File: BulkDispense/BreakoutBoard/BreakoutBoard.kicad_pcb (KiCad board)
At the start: 2 copper layers, 80 x 80 mm, 30 parts, among them J1 PS, J10 R0~R5, J11 WL1, J12 WL2, J13 DigitalOUT 0~3, J14 DigitalOUT 4~7, J15 WB1, J16 WB2, J17 AnalogIOs, J18 WB-MV1&2, J19 WB-MV3&4, J2 MV1&2, J20 FS1, J21 FS2~FS4, J22 WB-MV5&6, J24 LDS, J3 MV3&4, J4 RV1~4, J5 PCV, J6 FS1, J7 FS3, J8 FS2, J9 FS4

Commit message: Add updated layout
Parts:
- J11, J12, J15, J16, J22: footprint PartsLibrary:CONN_37203-62A3-003PL_3MM -> PartsLibrary:CONN_37204-62A3-004PL_3MM
- moved J22 2.27 mm to (142.6, 45.3)
- moved J16 2.05 mm to (152.5, 47.8)
- moved J15 2.00 mm to (152.5, 38.7)
- moved J11 1.16 mm to (169.2, 38.7)
- moved J12 1.15 mm to (169.2, 47.8)
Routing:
- net /R4_OUT: track 12.5 -> 19.6 mm
- net /AI4: track 97.8 -> 95.9 mm
- net /R0_OUT: track 52.4 -> 53.5 mm
- net +24V: track 159.2 -> 158.3 mm
- net /R5_OUT: track 9.38 -> 8.58 mm
- net /R2_OUT: track 52.2 -> 53.0 mm
- net GND: track 37.6 -> 36.8 mm
- net /AI7: track 90.9 -> 91.6 mm
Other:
- board text added: "v 1.1"
- board text removed: "v 1.0"

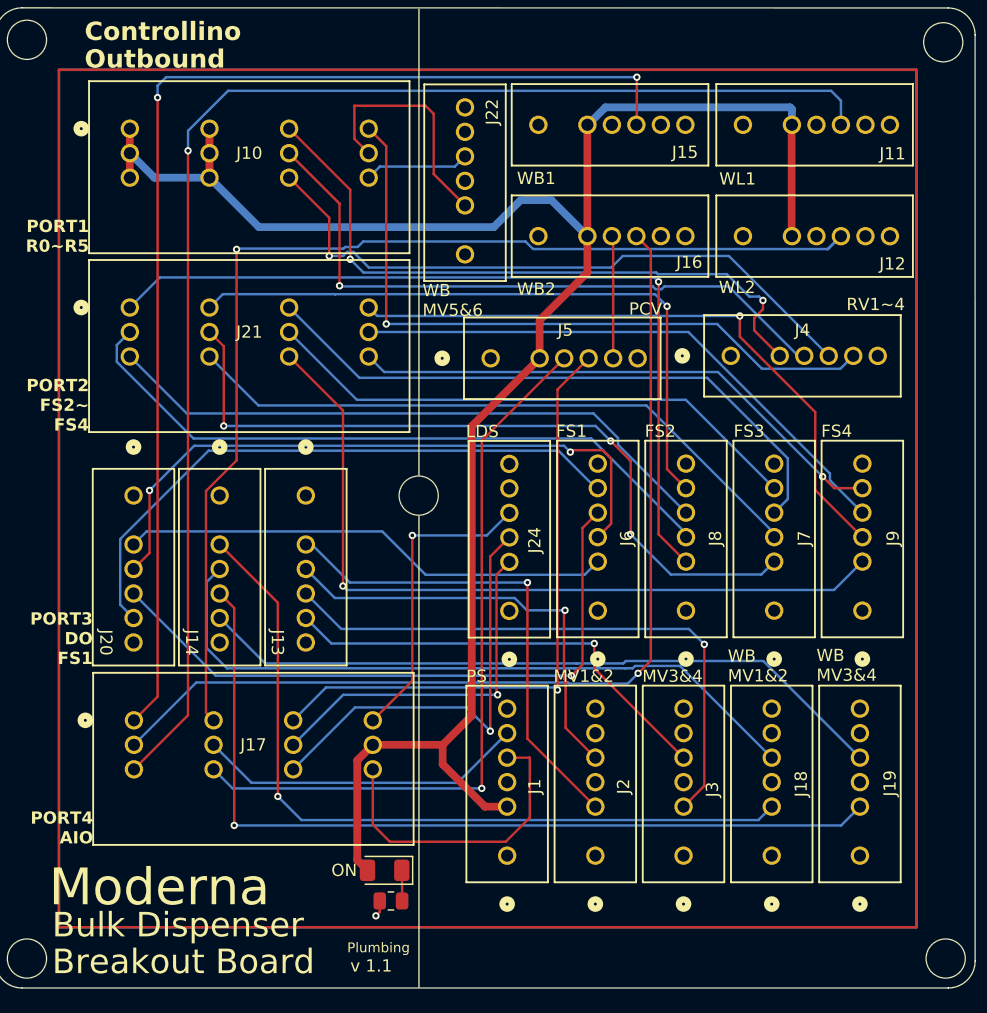
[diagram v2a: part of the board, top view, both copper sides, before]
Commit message: Add PCB Revisions
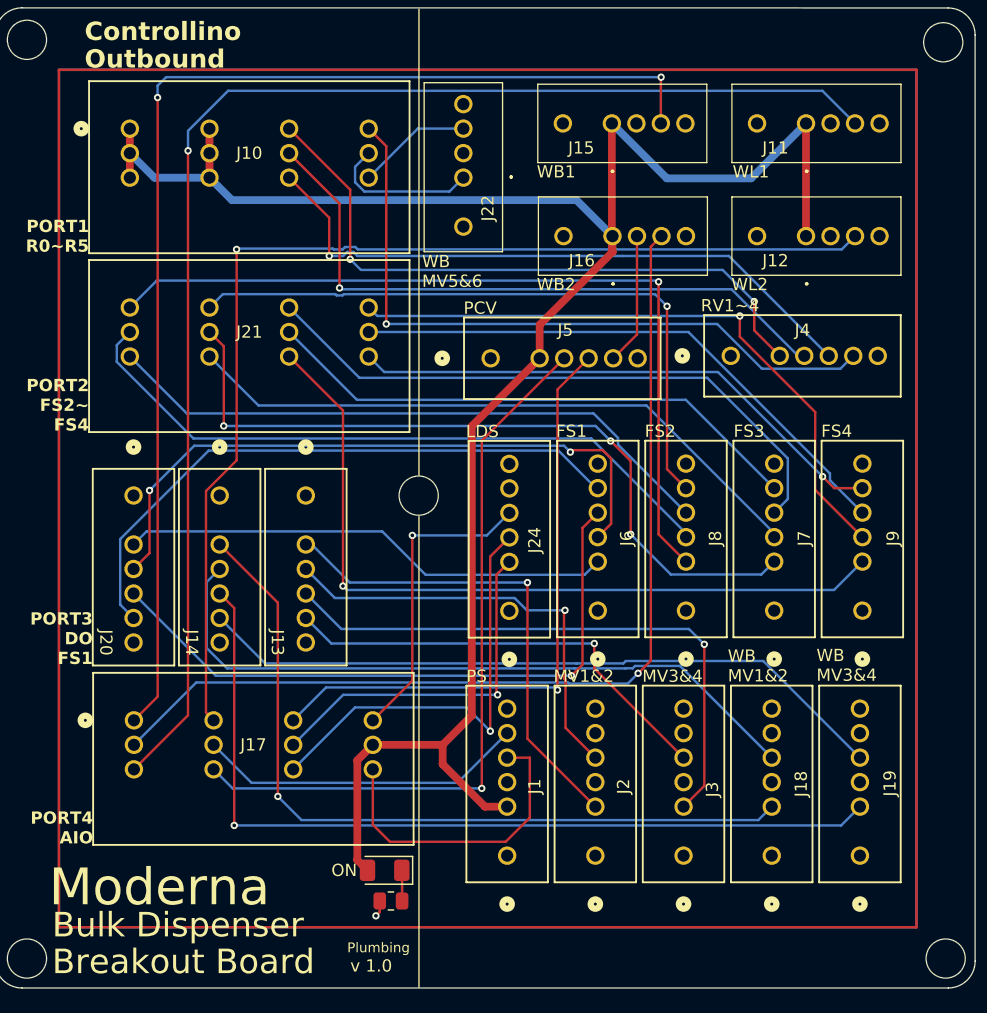
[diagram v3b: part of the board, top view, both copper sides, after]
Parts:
- J11, J12, J15, J16, J22: footprint PartsLibrary:CONN_37204-62A3-004PL_3MM -> PartsLibrary:CONN_37203-62A3-003PL_3MM
- moved J22 2.27 mm to (142.4, 43.0)
- moved J16 2.05 mm to (154.6, 47.8)
- moved J15 2.00 mm to (154.6, 38.6)
- moved J11 1.16 mm to (170.4, 38.6)
- moved J12 1.15 mm to (170.4, 47.8)
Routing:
- net /R4_OUT: track 19.6 -> 12.5 mm
- net +24V: track 158.3 -> 161.9 mm
- net /AI4: track 95.9 -> 97.8 mm
- net /R0_OUT: track 53.5 -> 52.4 mm
- net /R5_OUT: track 8.58 -> 9.38 mm
- net /R2_OUT: track 53.0 -> 52.2 mm
- net GND: track 36.8 -> 37.6 mm
- net /AI7: track 91.6 -> 90.9 mm
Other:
- board text added: "v 1.0"
- board text removed: "v 1.1"

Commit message: Add New Design
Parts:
- removed J10: R0~R5, PartsLibrary:CONN_37212-62M3-003PL_3MM
- removed J13: DigitalOUT 0~3, PartsLibrary:CONN_37204-62A3-004PL_3MM
- removed J14: DigitalOUT 4~7, PartsLibrary:CONN_37204-62A3-004PL_3MM
- removed J17: AnalogIOs, PartsLibrary:CONN_37212-62M3-003PL_3MM
- removed J18: WB-MV1&2, PartsLibrary:CONN_37204-62A3-004PL_3MM
- removed J19: WB-MV3&4, PartsLibrary:CONN_37204-62A3-004PL_3MM
- removed J2: MV1&2, PartsLibrary:CONN_37204-62A3-004PL_3MM
- removed J21: FS2~FS4, PartsLibrary:CONN_37212-62M3-003PL_3MM
- removed J22: WB-MV5&6, PartsLibrary:CONN_37203-62A3-003PL_3MM
- removed J3: MV3&4, PartsLibrary:CONN_37204-62A3-004PL_3MM
- removed J6: FS1, PartsLibrary:CONN_37204-62A3-004PL_3MM
- removed J7: FS3, PartsLibrary:CONN_37204-62A3-004PL_3MM
- removed J8: FS2, PartsLibrary:CONN_37204-62A3-004PL_3MM
- removed J9: FS4, PartsLibrary:CONN_37204-62A3-004PL_3MM
- added D3: LED, LED_SMD:LED_0201_0603Metric, F.Cu at (251.3, 70.7)
- added D4: LED, LED_SMD:LED_0201_0603Metric, F.Cu at (251.3, 72.5)
- added J36: WB-MV6, PartsLibrary:CONN_37203-62A3-003PL_3MM, F.Cu at (207.1, 88.4)
- added J37: RV1, PartsLibrary:CONN_37203-62A3-003PL_3MM, F.Cu at (222.1, 38.3)
- added J38: RV3, PartsLibrary:CONN_37203-62A3-003PL_3MM, F.Cu at (222.1, 46.7)
- added J39: RV2, PartsLibrary:CONN_37203-62A3-003PL_3MM, F.Cu at (222.1, 55.0)
- added J40: RV4, PartsLibrary:CONN_37203-62A3-003PL_3MM, F.Cu at (222.1, 63.4)
- added J41: MV1, PartsLibrary:CONN_37203-62A3-003PL_3MM, F.Cu at (222.1, 71.7)
- added J42: MV2, PartsLibrary:CONN_37203-62A3-003PL_3MM, F.Cu at (222.1, 80.1)
- added J43: MV3, PartsLibrary:CONN_37203-62A3-003PL_3MM, F.Cu at (222.1, 88.4)
- added J44: MV4, PartsLibrary:CONN_37203-62A3-003PL_3MM, F.Cu at (237.1, 38.3)
- added J45: WB-MV1, PartsLibrary:CONN_37203-62A3-003PL_3MM, F.Cu at (237.1, 46.7)
- added J46: WB-MV3, PartsLibrary:CONN_37203-62A3-003PL_3MM, F.Cu at (237.1, 55.0)
- added J47: WB-MV2, PartsLibrary:CONN_37203-62A3-003PL_3MM, F.Cu at (237.1, 63.4)
- added J48: WB-MV4, PartsLibrary:CONN_37203-62A3-003PL_3MM, F.Cu at (237.1, 71.7)
- added JP1: Jumper_2_Open, Connector_PinHeader_1.00mm:PinHeader_1x02_P1.00mm_Vertical, F.Cu at (247.1, 52.2)
- added JP2: Jumper_2_Open, Connector_PinHeader_1.00mm:PinHeader_1x02_P1.00mm_Vertical, F.Cu at (250.5, 52.2)
- added JP3: Jumper_2_Open, Connector_PinHeader_1.00mm:PinHeader_1x02_P1.00mm_Vertical, F.Cu at (253.8, 52.2)
- added JP4: Jumper_2_Open, Connector_PinHeader_1.00mm:PinHeader_1x02_P1.00mm_Vertical, F.Cu at (257.2, 52.2)
- added JP5: Jumper_2_Open, Connector_PinHeader_1.00mm:PinHeader_1x02_P1.00mm_Vertical, F.Cu at (260.5, 52.2)
- added JP6: Jumper_2_Open, Connector_PinHeader_1.00mm:PinHeader_1x02_P1.00mm_Vertical, F.Cu at (247.1, 56.2)
- added JP7: Jumper_2_Open, Connector_PinHeader_1.00mm:PinHeader_1x02_P1.00mm_Vertical, F.Cu at (250.5, 56.2)
- added JP8: Jumper_2_Open, Connector_PinHeader_1.00mm:PinHeader_1x02_P1.00mm_Vertical, F.Cu at (253.8, 56.2)
- added R3: R, Resistor_SMD:R_0805_2012Metric, F.Cu at (247.7, 72.5)
- added R4: R, Resistor_SMD:R_0805_2012Metric, F.Cu at (247.7, 75.5)
- added U1: TCA9548APWR, Package_SO:TSSOP-24_4.4x7.8mm_P0.65mm, F.Cu at (250.2, 63.4)
- added U2: LMR51430, Package_TO_SOT_SMD:SOT-23-6, F.Cu at (257.1, 61.1)
- added U3: LMR51430, Package_TO_SOT_SMD:SOT-23-6, F.Cu at (257.1, 65.8)
- added U4: TVS2700DRV, Package_SON:WSON-6-1EP_2x2mm_P0.65mm_EP1x1.6mm, F.Cu at (254.6, 70.0)
- D1: footprint LED_SMD:LED_1206_3216Metric -> LED_SMD:LED_0201_0603Metric
- J20: value FS1 -> WB1; footprint PartsLibrary:CONN_37204-62A3-004PL_3MM -> PartsLibrary:CONN_37203-62A3-003PL_3MM
- J24: value LDS -> WB-MV5; footprint PartsLibrary:CONN_37204-62A3-004PL_3MM -> PartsLibrary:CONN_37203-62A3-003PL_3MM
- J4: value RV1~4 -> Signal; footprint PartsLibrary:CONN_37204-62A3-004PL_3MM -> PartsLibrary:CONN26_D13-ST-BK_SUL
- moved J1 120.1 mm to (252.3, 38.6), turned to 0 degrees
- moved D1 119.3 mm to (251.3, 69.0), turned to 0 degrees
- moved R1 115.8 mm to (247.7, 69.6), turned to 0 degrees
- moved J5 104.3 mm to (252.3, 46.6)
- moved J20 91.6 mm to (207.1, 71.7), turned to 0 degrees
- moved J4 63.0 mm to (110.3, 82.4), turned to 90 degrees
- moved J24 61.2 mm to (207.1, 80.1), turned to 0 degrees
- moved J15 55.1 mm to (207.1, 55.0)
- moved J16 54.8 mm to (207.1, 63.4)
- moved J12 36.7 mm to (207.1, 46.7)
- moved J11 36.7 mm to (207.1, 38.3)
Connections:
- J20 pad 1: /FS1-1 -> +5V
- J20 pad 2: /FS1-2 -> GND
- J20 pad 3: /FS1-3 -> /LDS
- J24 pad 1: /LDS-5V -> /R4_OUT
- J24 pad 2: /LDS-GND -> unconnected-(J24-Pin_2-Pad2)
- J24 pad 3: /LDS -> GND
- J4 pad 1: /R0_OUT -> +24V
- J4 pad 2: /R1_OUT -> GND
- J4 pad 3: /R2_OUT -> /R0_OUT
- J4 pad 4: /R3_OUT -> /R1_OUT
- J4 pad 5: (no net) -> /R2_OUT
- J4 pad 6: (no net) -> /R3_OUT
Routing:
- net +24V: track 161.9 -> 0.00 mm
- net /AI6: track 110.9 -> 0.00 mm, vias 1 -> 0
- net /AI4: track 97.8 -> 0.00 mm, vias 2 -> 0
- net /AI7: track 90.9 -> 0.00 mm, vias 1 -> 0
- net /AI5: track 80.1 -> 0.00 mm, vias 1 -> 0
- net /DO6: track 71.1 -> 0.00 mm, vias 1 -> 0
- net /FS2-1: track 67.9 -> 0.00 mm, vias 1 -> 0
- net /DO4: track 64.1 -> 0.00 mm, vias 1 -> 0
- net /FS4-1: track 64.1 -> 0.00 mm, vias 1 -> 0
- net /FS3-1: track 62.0 -> 0.00 mm, vias 3 -> 0
- net /AI13: track 60.4 -> 0.00 mm, vias 1 -> 0
- net /DO7: track 57.2 -> 0.00 mm
- net /DO5: track 56.9 -> 0.00 mm
- net /R3_OUT: track 56.6 -> 0.00 mm, vias 1 -> 0
- net /FS2-2: track 55.5 -> 0.00 mm
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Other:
- board text removed: "LDS"
- board text removed: "PORT1 R0~R5"
- board text removed: "PORT2 FS2~ FS4"
- board text removed: "PORT3 DO FS1"
- board text removed: "PORT4 AIO"
- board text removed: "WB MV1&2"
- board text removed: "WB MV3&4"
- board text removed: "WB MV5&6"
- board text removed: "WB1"
- board text removed: "WB2"
- board text removed: "WL1"
- board text removed: "WL2"

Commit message: Start PCB Routing
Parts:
- removed JP1, JP2, JP3, JP4, JP5, JP6, JP7, JP8: Jumper_2_Open, Connector_PinHeader_1.00mm:PinHeader_1x02_P1.00mm_Vertical
- added 24V: TestPoint, TestPoint:TestPoint_THTPad_D1.0mm_Drill0.5mm, F.Cu at (113.7, 91.8)
- added 3V3: TestPoint, TestPoint:TestPoint_THTPad_D1.0mm_Drill0.5mm, F.Cu at (139.6, 87.3)
- added 5V: TestPoint, TestPoint:TestPoint_THTPad_D1.0mm_Drill0.5mm, F.Cu at (123.5, 87.3)
- added C1: 10uF, Capacitor_SMD:C_01005_0402Metric, F.Cu at (73.0, 72.4)
- added C10: 22uF, Capacitor_SMD:C_0805_2012Metric, F.Cu at (124.5, 92.1)
- added C11: 22uF, Capacitor_SMD:C_0805_2012Metric, F.Cu at (140.5, 91.1)
- added C2: 0.1uF, Capacitor_SMD:C_01005_0402Metric, F.Cu at (129.9, 95.2)
- added C3: 4.7uF, Capacitor_SMD:C_0805_2012Metric, F.Cu at (119.8, 90.2)
- added C4: 22uF, Capacitor_SMD:C_0805_2012Metric, F.Cu at (124.5, 90.1)
- added C5: 4.7uF, Capacitor_SMD:C_0805_2012Metric, F.Cu at (129.9, 89.9)
- added C6: 0.1uF, Capacitor_SMD:C_01005_0402Metric, F.Cu at (146.1, 95.4)
- added C7: 22uF, Capacitor_SMD:C_0805_2012Metric, F.Cu at (140.5, 93.1)
- added C8: 4.7uF, Capacitor_SMD:C_0805_2012Metric, F.Cu at (119.8, 92.2)
- added C9: 4.7uF, Capacitor_SMD:C_0805_2012Metric, F.Cu at (129.9, 92.1)
- added GND: TestPoint, TestPoint:TestPoint_THTPad_1.0x1.0mm_Drill0.5mm, F.Cu at (106.6, 91.9)
- added J10: FS1, Connector_Molex:Molex_PicoBlade_53047-0610_1x06_P1.25mm_Vertical, F.Cu at (168.9, 83.7)
- added J13: FS2, Connector_Molex:Molex_PicoBlade_53047-0610_1x06_P1.25mm_Vertical, F.Cu at (168.9, 88.9)
- added J14: FS3, Connector_Molex:Molex_PicoBlade_53047-0610_1x06_P1.25mm_Vertical, F.Cu at (168.9, 94.2)
- added J17: FS4, Connector_Molex:Molex_PicoBlade_53047-0610_1x06_P1.25mm_Vertical, F.Cu at (168.9, 99.4)
- added L1: 6.8uH, Inductor_SMD:L_Bourns_SRP7028A_7.3x6.6mm, F.Cu at (121.5, 97.7)
- added L2: 5.6uH, PartsLibrary:IND_IHLP-2020CZ, F.Cu at (139.1, 98.1)
- added R10: 4.7k, Resistor_SMD:R_0402_1005Metric, F.Cu at (70.4, 76.6)
- added R11: 0, Resistor_SMD:R_0402_1005Metric, F.Cu at (77.2, 69.9)
- added R12: 0, Resistor_SMD:R_0402_1005Metric, F.Cu at (77.2, 71.9)
- added R13: 0, Resistor_SMD:R_0402_1005Metric, F.Cu at (77.2, 73.9)
- added R14: 4.7k, Resistor_SMD:R_0402_1005Metric, F.Cu at (86.0, 65.4)
- added R15: 4.7k, Resistor_SMD:R_0402_1005Metric, F.Cu at (86.0, 67.4)
- added R16: 4.7k, Resistor_SMD:R_0402_1005Metric, F.Cu at (86.0, 69.4)
- added R17: 4.7k, Resistor_SMD:R_0402_1005Metric, F.Cu at (86.0, 71.4)
- added R18: 4.7k, Resistor_SMD:R_0402_1005Metric, F.Cu at (88.9, 65.4)
- added R19: 4.7k, Resistor_SMD:R_0402_1005Metric, F.Cu at (88.9, 67.4)
- added R2: 10k, Resistor_SMD:R_0402_1005Metric, F.Cu at (70.4, 72.6)
- added R20: 4.7k, Resistor_SMD:R_0402_1005Metric, F.Cu at (88.9, 69.4)
- added R21: 4.7k, Resistor_SMD:R_0402_1005Metric, F.Cu at (88.9, 71.4)
- added R22: 4.7k, Resistor_SMD:R_0402_1005Metric, F.Cu at (91.8, 65.4)
- added R23: 4.7k, Resistor_SMD:R_0402_1005Metric, F.Cu at (91.8, 67.4)
- added R24: 4.7k, Resistor_SMD:R_0402_1005Metric, F.Cu at (91.8, 69.4)
- added R25: 4.7k, Resistor_SMD:R_0402_1005Metric, F.Cu at (91.8, 71.4)
- added R26: 4.7k, Resistor_SMD:R_0402_1005Metric, F.Cu at (94.7, 65.4)
- added R27: 4.7k, Resistor_SMD:R_0402_1005Metric, F.Cu at (94.7, 67.4)
- added R28: 4.7k, Resistor_SMD:R_0402_1005Metric, F.Cu at (94.7, 69.4)
- added R29: 4.7k, Resistor_SMD:R_0402_1005Metric, F.Cu at (94.7, 71.4)
- added R5: 100k, Resistor_SMD:R_0603_1608Metric, F.Cu at (132.2, 96.9)
- added R6: 13.7k, Capacitor_SMD:C_0603_1608Metric, F.Cu at (132.2, 98.4)
- added R7: 100k, Resistor_SMD:R_0603_1608Metric, F.Cu at (148.6, 96.8)
- added R8: 22.1k, Resistor_SMD:R_0603_1608Metric, F.Cu at (148.6, 98.3)
- added R9: 4.7k, Resistor_SMD:R_0402_1005Metric, F.Cu at (70.4, 74.6)
- R1: value R -> 2.2k
- R3: value R -> 330
- R4: value R -> 150
- moved D4 146.5 mm to (107.3, 99.5), turned to 180 degrees
- moved D3 146.4 mm to (107.3, 97.0), turned to 180 degrees
- moved D1 146.3 mm to (107.3, 94.4), turned to 180 degrees
- moved U1 140.2 mm to (111.8, 41.1)
- moved R1 139.8 mm to (110.1, 94.6)
- moved R3 139.8 mm to (110.1, 97.3)
- moved R4 139.7 mm to (110.1, 99.8)
- moved U4 139.2 mm to (116.8, 89.2), turned to -90 degrees
- moved U2 133.4 mm to (128.7, 97.4)
- moved U3 116.7 mm to (144.8, 97.4)
- moved J4 3.14 mm to (108.0, 84.5)
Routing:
- net +24V: track 0.00 -> 108.7 mm, vias 0 -> 1
- net +3.3V: track 0.00 -> 49.4 mm, vias 0 -> 1
- net GND: track 0.00 -> 39.2 mm, vias 0 -> 14
- net +5V: track 0.00 -> 33.7 mm, vias 0 -> 1
- net Net-(U2-SW): track 0.00 -> 20.5 mm, vias 0 -> 2
- net Net-(U3-SW): track 0.00 -> 19.7 mm, vias 0 -> 2
- net Net-(U2-FB): track 0.00 -> 4.46 mm
- net Net-(U3-FB): track 0.00 -> 3.34 mm
- net Net-(D3-K): track 0.00 -> 2.20 mm
- net Net-(D1-K): track 0.00 -> 1.85 mm
- net Net-(D4-K): track 0.00 -> 1.77 mm
- net Net-(U3-CB): track 0.00 -> 1.53 mm
- net Net-(U2-CB): track 0.00 -> 1.39 mm
- net /LDS: vias 1 -> 0
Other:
- board text added: "24V"
- board text added: "3V3"
- board text added: "5V"
- board text added: "v 2.0"
- board text removed: "ON"
- board text removed: "v 1.0"

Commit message: Start I2C Layout
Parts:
- removed R11, R12, R13: 0, Resistor_SMD:R_0402_1005Metric
- removed R21, R22, R23, R24, R25, R26, R27: 4.7k, Resistor_SMD:R_0402_1005Metric
- added R30: 4.7k, Resistor_SMD:R_0402_1005Metric, F.Cu at (106.4, 47.2)
- moved J1 113.9 mm to (140.0, 57.3), turned to 90 degrees
- moved J5 104.3 mm to (148.6, 57.1), turned to 90 degrees
- moved J20 84.2 mm to (123.2, 77.8), turned to 90 degrees
- moved J17 69.5 mm to (145.6, 34.0), turned to -90 degrees
- moved J14 67.6 mm to (138.1, 34.0), turned to -90 degrees
- moved J10 67.5 mm to (123.2, 34.0), turned to -90 degrees
- moved J13 67.0 mm to (130.6, 34.0), turned to -90 degrees
- moved R20 62.7 mm to (143.3, 38.1), turned to 90 degrees
- moved R19 61.2 mm to (141.3, 35.9), turned to -90 degrees
- moved R18 59.1 mm to (141.3, 38.1), turned to 90 degrees
- moved R28 59.0 mm to (143.3, 35.9), turned to -90 degrees
- moved R2 58.5 mm to (117.4, 37.7), turned to 180 degrees
- moved R17 55.2 mm to (128.3, 36.0), turned to -90 degrees
- moved R10 53.6 mm to (116.3, 48.8), turned to -90 degrees
- moved R16 52.6 mm to (128.3, 38.2), turned to 90 degrees
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- renumbered 24V to TP1, GND to TP2, 3V3 to TP4, 5V to TP5
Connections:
- R29 pad 1: +3.3V -> /SC4
- R29 pad 2: /SC4 -> +3.3V
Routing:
- net +3.3V: track 49.4 -> 176.5 mm, vias 1 -> 3
- net /FS4-SCL: track 0.00 -> 43.3 mm
- net /FS4-SDA: track 0.00 -> 41.6 mm
- net /FS3-SDA: track 0.00 -> 35.7 mm
- net /FS3-SCL: track 0.00 -> 35.4 mm
- net /LDS: track 0.00 -> 32.9 mm
- net /FS2-SDA: track 0.00 -> 23.2 mm
- net /FS2-SCL: track 0.00 -> 22.1 mm
- net /FS1-SDA: track 0.00 -> 16.7 mm
- net /FS1-SCL: track 0.00 -> 16.0 mm
- net /SDA: track 0.00 -> 13.1 mm
- net /SCL: track 0.00 -> 11.2 mm
- net +5V: track 33.7 -> 44.3 mm
- net GND: track 39.2 -> 45.3 mm, vias 14 -> 19
- net Net-(U1-~{RESET}): track 0.00 -> 4.74 mm
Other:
- board text added: "I2C"
- board text removed: "Controllino"
- board text removed: "Outbound"

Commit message: Finalized Draft - BreakoutBoard
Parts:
- removed R29, R30: 4.7k, Resistor_SMD:R_0402_1005Metric
- added G***: LOGO, LOGO, F.Cu at (123.1, 70.5)
- C2, C6: footprint Capacitor_SMD:C_01005_0402Metric -> Capacitor_SMD:C_0603_1608Metric
- J20: value WB1 -> LDS
- J24: value WB-MV5 -> WB-MV1
- J36: value WB-MV6 -> WB-MV2
- moved D3 93.0 mm to (173.6, 31.8)
- moved R3 91.0 mm to (174.9, 33.3)
- moved J48 83.2 mm to (142.1, 100.3), turned to 90 degrees
- moved J46 82.6 mm to (148.9, 100.3), turned to 90 degrees
- moved D4 82.4 mm to (154.5, 31.9)
- moved R4 80.4 mm to (155.7, 33.6)
- moved J44 75.6 mm to (169.4, 100.3), turned to 90 degrees
- moved J45 75.4 mm to (162.4, 100.3), turned to 90 degrees
- moved C2 73.4 mm to (174.2, 36.7)
- moved R6 73.0 mm to (176.2, 40.1)
- moved R5 73.0 mm to (176.2, 38.7)
- moved J47 73.0 mm to (155.7, 100.3), turned to 90 degrees
- moved L1 72.8 mm to (165.2, 39.5)
- moved C10 72.8 mm to (168.1, 33.9)
- moved C4 72.8 mm to (168.1, 31.8)
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- renumbered J17 to FS1, J14 to FS2, J13 to FS3, J10 to FS4
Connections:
- J4 pad 10: /DO1 -> /AI12
- J4 pad 11: /DO2 -> /AI13
- J4 pad 12: /DO3 -> /AO0
- J4 pad 13: /DO4 -> /R0_OUT
- J4 pad 14: /DO5 -> /R1_OUT
- J4 pad 15: /DO6 -> /R2_OUT
- J4 pad 16: /DO7 -> /R3_OUT
- J4 pad 17: /AI4 -> /R4_OUT
- J4 pad 18: /AI5 -> /R5_OUT
- J4 pad 19: /AI6 -> /DO0
- J4 pad 20: /AI7 -> /DO1
- J4 pad 21: /AI12 -> /DO2
- J4 pad 22: /AI13 -> /DO3
- J4 pad 23: /AO0 -> /DO4
- J4 pad 24: /LDS -> /DO5
- J4 pad 25: /SCL -> /DO6
- J4 pad 26: /SDA -> /DO7
- J4 pad 3: /R0_OUT -> /SDA
- J4 pad 4: /R1_OUT -> /SCL
- J4 pad 5: /R2_OUT -> /LDS
- J4 pad 6: /R3_OUT -> /AI4
- J4 pad 7: /R4_OUT -> /AI5
- J4 pad 8: /R5_OUT -> /AI6
- J4 pad 9: /DO0 -> /AI7
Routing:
- net /DO2: track 0.00 -> 86.3 mm
- net /R3_OUT: track 0.00 -> 84.2 mm
- net /DO3: track 0.00 -> 80.2 mm
- net +3.3V: track 176.5 -> 97.9 mm, vias 3 -> 2
- net /R4_OUT: track 0.00 -> 72.5 mm
- net /AI13: track 0.00 -> 72.3 mm
- net /AI12: track 0.00 -> 72.1 mm
- net /DO4: track 0.00 -> 70.2 mm
- net /AI4: track 0.00 -> 68.9 mm
- net /DO5: track 0.00 -> 68.3 mm, vias 0 -> 1
- net /R5_OUT: track 0.00 -> 68.3 mm
- net /AO0: track 0.00 -> 67.8 mm
- net /R1_OUT: track 0.00 -> 60.7 mm, vias 0 -> 1
- net /AI5: track 0.00 -> 59.3 mm
- net /R0_OUT: track 0.00 -> 58.7 mm
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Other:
- board text added: "LDS"
- board text added: "MV1"
- board text added: "MV2"
- board text added: "MV3"
- board text added: "MV4"
- board text added: "PCV"
- board text added: "PS"
- board text added: "RV1"
- board text added: "RV2"
- board text added: "RV3"
- board text added: "RV4"
- board text added: "TP1"
- board text added: "WB-MV1"
- board text added: "WB-MV2"
- board text added: "WB-MV3"
- board text added: "WB-MV4"
- board text added: "WB1"
- board text added: "WB2"
- board text added: "WL1"
- board text added: "WL2"
- board text removed: "Moderna"
- board text removed: "Plumbing"

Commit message: Final Design Changes for Both Boards
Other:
- board text added: "Plumbing"
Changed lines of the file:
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@@
 		(layer "Edge.Cuts")
 	)
+	(gr_text "Plumbing"
+		(at 131.8768 80.8228 90)
+		(layer "F.SilkS")
+		(effects
+			(font
+				(size 1.016 1)
+				(thickness 0.153)
+			)
+			(justify left bottom)
+		)
+	)
 	(gr_text "WB-MV2"
 		(at 132.8928 103.160724 90)
@@
 	)
 	(gr_text "v 2.0"
-		(at 130.2764 67.9196 90)
+		(at 130.2004 67.6656 90)
 		(layer "F.SilkS")
 		(effects
@@
 	)
 	(gr_text "Breakout Board"
-		(at 130.2032 80.8188 90)
+		(at 130.302 80.8228 90)
 		(layer "F.SilkS")
 		(effects
@@
 	)
 	(gr_text "Bulk Dispenser"
-		(at 128.7272 80.8188 90)
+		(at 128.7272 80.8228 90)
 		(layer "F.SilkS")
 		(effects
@@
 	)
 	(group ""
-		(members "2dce61c2-283b-4acd-b3df-0613b3b5c2a0" "6c470501-d674-4749-93c2-2553a0ad65cf"
-			"f6bfeb69-9554-436d-b090-29551b7f3835" "fea23e74-3d27-446e-982d-fc6a39eb33bd"
+		(members "0515e593-0c95-46ad-86e6-3979619f12e1" "2dce61c2-283b-4acd-b3df-0613b3b5c2a0"
+			"6c470501-d674-4749-93c2-2553a0ad65cf" "f6bfeb69-9554-436d-b090-29551b7f3835"
+			"fea23e74-3d27-446e-982d-fc6a39eb33bd"
 		)
 	)
